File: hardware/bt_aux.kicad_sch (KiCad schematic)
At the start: 19 parts, among them J1 esp32_1, J2 AudioJack3, J2 esp32_2, U1 PCM5102A

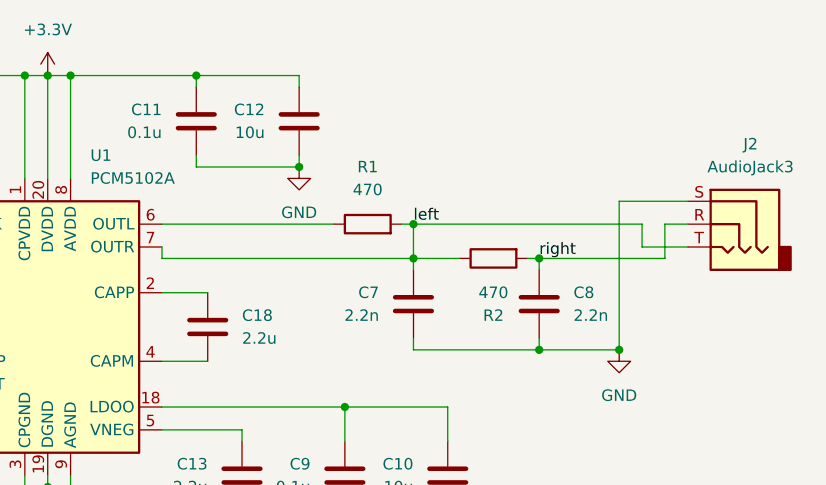
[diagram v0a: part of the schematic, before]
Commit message: update footprints, links, and price of components
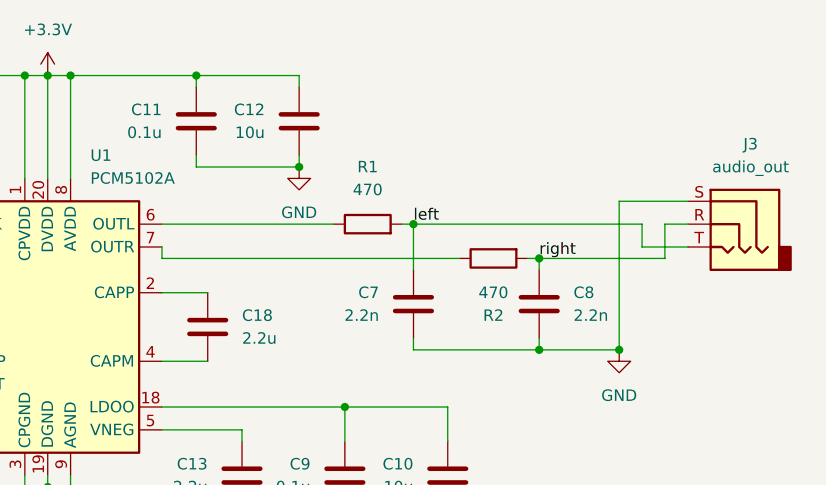
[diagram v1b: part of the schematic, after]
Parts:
- C10, C12, C15, C17: footprint (none) -> C_0805_2012Metric; Link (none) -> https://jlcpcb.com/partdetail/MurataElectronics-GRM21BR61E1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; Unit Price (none) -> $0.0168
- C11, C14, C16, C9: footprint (none) -> C_0805_2012Metric; Link (none) -> https://jlcpcb.com/partdetail/Walsin_TechCorp-0805B104K101C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; Unit Price (none) -> $0.0045
- C13, C18: footprint (none) -> C_0805_2012Metric; Link (none) -> https://jlcpcb.com/partdetail/19814-CL21B225KAFNNNE/C19110; Unit Price (none) -> $0.0128
- C7, C8: footprint (none) -> C_0805_2012Metric; Link (none) -> https://jlcpcb.com/partdetail/Walsin_TechCorp-0805N222J101C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; Unit Price (none) -> $0.0188
- J1, J2: footprint (none) -> Connector_PinSocket_2.54mm:PinSocket_1x15_P2.54mm_Vertical; Link (none) -> https://jlcpcb.com/partdetail/Hctl-PM254_1_15_Z_85/C2897378; Unit Price (none) -> $0.2109
- J3: renamed from J2; value AudioJack3 -> audio_out; footprint (none) -> audio-jack:BOOMELE_PJ-320B; Link (none) -> https://jlcpcb.com/partdetail/boomele_boom_Precision_elec-C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; Unit Price (none) -> $0.0491
- R1, R2: footprint (none) -> R_0805_2012Metric; Link (none) -> https://jlcpcb.com/partdetail/Kamaya-RMC1_10471JTP/C908864; Unit Price (none) -> $0.0019
- R3: footprint (none) -> R_0805_2012Metric; Link (none) -> https://jlcpcb.com/partdetail/18102-0805W8F1002T5E/C17414; Unit Price (none) -> $0.0013
- U1: Link (none) -> https://jlcpcb.com/partdetail/TexasInstruments-PCM5102APWR/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; Unit Price (none) -> $1.4820
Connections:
- net left: no longer R2.1, U1.7 (OUTR)
- new net: R2.1, U1.7 (OUTR)

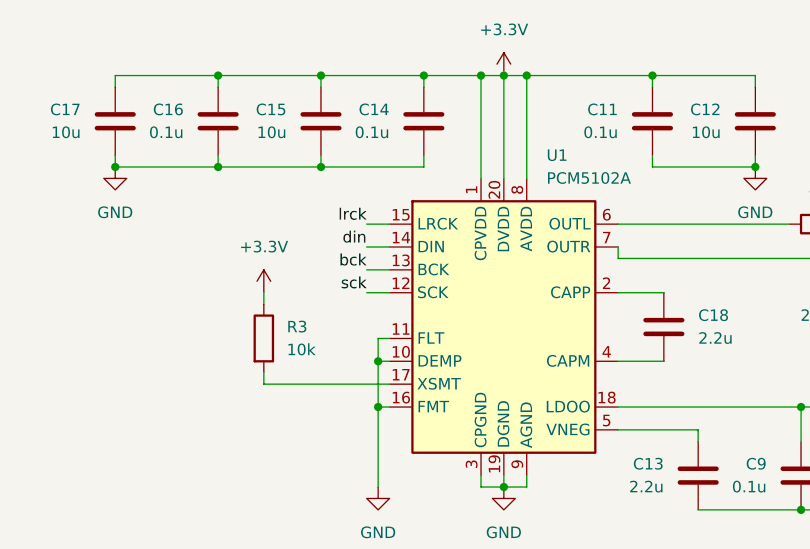
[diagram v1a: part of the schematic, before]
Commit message: change xsmt connection direct to avdd instead of pullup
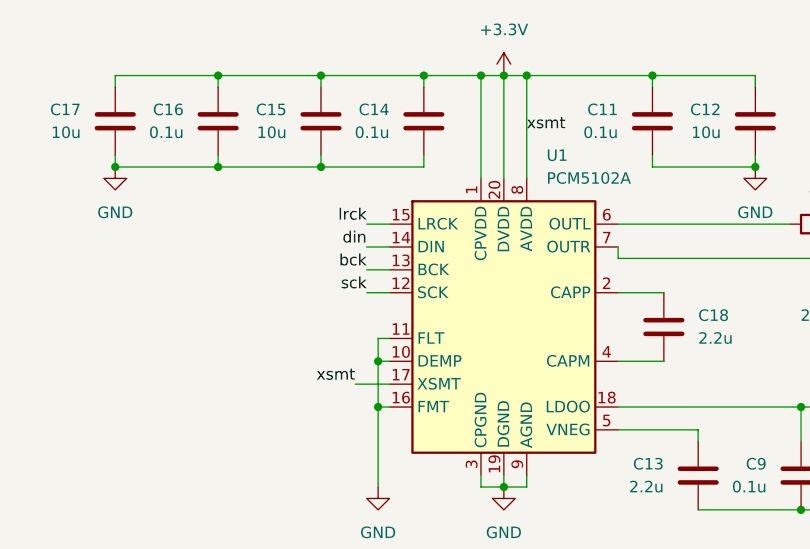
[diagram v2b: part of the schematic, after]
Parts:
- removed R3: 10k, R_0805_2012Metric, symbol Device:R
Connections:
- net +3.3V: now also U1.17 (XSMT)
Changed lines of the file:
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@@
+    (stroke (width 0) (type default))
+  )
+  (wire (pts (xy 144.78 91.44) (xy 148.59 91.44))
     (stroke (width 0) (type default))
   )
@@
     (stroke (width 0) (type default))
   )
-  (wire (pts (xy 134.62 91.44) (xy 148.59 91.44))
-    (stroke (width 0) (type default))
-  )
   (wire (pts (xy 146.05 81.28) (xy 148.59 81.28))
     (stroke (width 0) (type default))
@@
     (stroke (width 0) (type default))
   )
-  (wire (pts (xy 134.62 81.28) (xy 134.62 82.55))
-    (stroke (width 0) (type default))
-  )
   (wire (pts (xy 173.99 77.47) (xy 173.99 76.2))
     (stroke (width 0) (type default))
@@
     (stroke (width 0) (type default))
   )
-  (wire (pts (xy 134.62 90.17) (xy 134.62 91.44))
-    (stroke (width 0) (type default))
-  )
   (wire (pts (xy 227.33 73.66) (xy 201.93 73.66))
     (stroke (width 0) (type default))
@@
   (label "lrck" (at 46.99 88.9 180) (fields_autoplaced)
     (effects (font (size 1.27 1.27)) (justify right bottom))
+  )
+  (label "xsmt" (at 163.83 63.5 0) (fields_autoplaced)
+    (effects (font (size 1.27 1.27)) (justify left bottom))
   )
   (label "bck" (at 46.99 93.98 180) (fields_autoplaced)
@@
   )
   (label "din" (at 46.99 91.44 180) (fields_autoplaced)
+    (effects (font (size 1.27 1.27)) (justify right bottom))
+  )
+  (label "xsmt" (at 144.78 91.44 180) (fields_autoplaced)
     (effects (font (size 1.27 1.27)) (justify right bottom))
   )
@@
     )
   )
-  (symbol (lib_id "power:+3.3V") (at 134.62 81.28 0) (unit 1)
-    (in_bom yes) (on_board yes) (dnp no) (fields_autoplaced)
-    (property "Reference" "#PWR06" (at 134.62 85.09 0)
-      (effects (font (size 1.27 1.27)) hide)
-    )
-    (property "Value" "+3.3V" (at 134.62 76.2 0)
-      (effects (font (size 1.27 1.27)))
-    )
-    (property "Footprint" "" (at 134.62 81.28 0)
-      (effects (font (size 1.27 1.27)) hide)
-    )
-    (property "Datasheet" "" (at 134.62 81.28 0)
-      (effects (font (size 1.27 1.27)) hide)
-    )
-    (pin "1")
-    (instances
-      (project "bt_aux"
-        (path "/cca713bf-7872-426b-918e-02310faf0ed4"
-          (reference "#PWR06") (unit 1)
-        )
-      )
-    )
-  )
   (symbol (lib_id "Device:C") (at 129.54 62.23 0) (unit 1)
     (in_bom yes) (on_board yes) (dnp no)
@@
         )
       )
-    )
-  )
-  (symbol (lib_id "Device:R") (at 134.62 86.36 0) (unit 1)
-    (in_bom yes) (on_board yes) (dnp no) (fields_autoplaced)
-    (property "Reference" "R3" (at 137.16 85.09 0)
-      (effects (font (size 1.27 1.27)) (justify left))
-    )
-    (property "Value" "10k" (at 137.16 87.63 0)
-      (effects (font (size 1.27 1.27)) (justify left))
-    )
-    (property "Footprint" "R_0805_2012Metric" (at 132.842 86.36 90)
-      (effects (font (size 1.27 1.27)) hide)
-    )
-    (property "Datasheet" "~" (at 134.62 86.36 0)
-      (effects (font (size 1.27 1.27)) hide)
-    )
-    (property "Link" "https://jlcpcb.com/partdetail/18102-0805W8F1002T5E/C17414" (at 134.62 86.36 0)
-      (effects (font (size 1.27 1.27)) hide)
-    )
-    (property "Unit Price" " $0.0013 " (at 134.62 86.36 0)
-      (effects (font (size 1.27 1.27)) hide)
-    )
-    (pin "2")
-    (pin "1")
-    (instances
-      (project "bt_aux"
-        (path "/cca713bf-7872-426b-918e-02310faf0ed4"
-          (reference "R3") (unit 1)
-        )
-      )

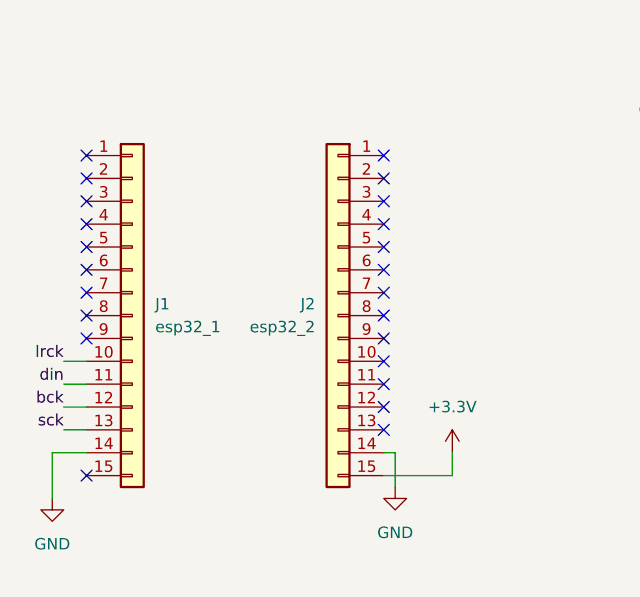
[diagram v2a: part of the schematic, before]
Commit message: add copper pours and rest of connections to headers
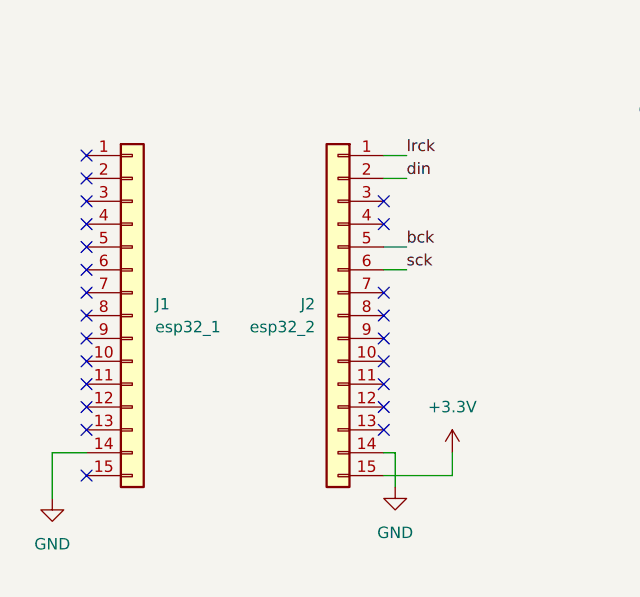
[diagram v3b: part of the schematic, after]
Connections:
- net bck: now also J2.5 (Pin_5); no longer J1.12 (Pin_12)
- net din: now also J2.2 (Pin_2); no longer J1.11 (Pin_11)
- net lrck: now also J2.1 (Pin_1); no longer J1.10 (Pin_10)
- net sck: now also J2.6 (Pin_6); no longer J1.13 (Pin_13)
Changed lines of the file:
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@@
   )
   (no_connect (at 82.55 96.52))
-  (no_connect (at 82.55 66.04))
   (no_connect (at 82.55 91.44))
   (no_connect (at 82.55 86.36))
@@
   (no_connect (at 82.55 93.98))
   (no_connect (at 49.53 78.74))
+  (no_connect (at 49.53 93.98))
   (no_connect (at 49.53 81.28))
   (no_connect (at 82.55 83.82))
   (no_connect (at 49.53 86.36))
-  (no_connect (at 82.55 78.74))
-  (no_connect (at 82.55 68.58))
+  (no_connect (at 49.53 88.9))
   (no_connect (at 82.55 71.12))
   (no_connect (at 49.53 76.2))
@@
   (no_connect (at 82.55 73.66))
   (no_connect (at 82.55 88.9))
+  (no_connect (at 49.53 96.52))
   (no_connect (at 49.53 66.04))
+  (no_connect (at 49.53 91.44))
   (no_connect (at 49.53 71.12))
-  (no_connect (at 82.55 76.2))
   (wire (pts (xy 205.74 97.79) (xy 205.74 93.98))
     (stroke (width 0) (type default))
@@
     (stroke (width 0) (type default))
   )
-  (wire (pts (xy 46.99 96.52) (xy 49.53 96.52))
-    (stroke (width 0) (type default))
-  )
   (wire (pts (xy 146.05 78.74) (xy 148.59 78.74))
     (stroke (width 0) (type default))
@@
     (stroke (width 0) (type default))
   )
+  (wire (pts (xy 85.09 68.58) (xy 82.55 68.58))
+    (stroke (width 0) (type default))
+  )
   (wire (pts (xy 182.88 97.79) (xy 182.88 96.52))
     (stroke (width 0) (type default))
@@
     (stroke (width 0) (type default))
   )
+  (wire (pts (xy 85.09 78.74) (xy 82.55 78.74))
+    (stroke (width 0) (type default))
+  )
   (wire (pts (xy 173.99 96.52) (xy 182.88 96.52))
     (stroke (width 0) (type default))
@@
     (stroke (width 0) (type default))
   )
+  (wire (pts (xy 85.09 76.2) (xy 82.55 76.2))
+    (stroke (width 0) (type default))
+  )
   (wire (pts (xy 152.4 57.15) (xy 152.4 58.42))
     (stroke (width 0) (type default))
@@
     (stroke (width 0) (type default))
   )
-  (wire (pts (xy 46.99 93.98) (xy 49.53 93.98))
-    (stroke (width 0) (type default))
-  )
   (wire (pts (xy 158.75 102.87) (xy 158.75 101.6))
     (stroke (width 0) (type default))
@@
     (stroke (width 0) (type default))
   )
+  (wire (pts (xy 85.09 66.04) (xy 82.55 66.04))
+    (stroke (width 0) (type default))
+  )
   (wire (pts (xy 148.59 86.36) (xy 147.32 86.36))
     (stroke (width 0) (type default))
@@
     (stroke (width 0) (type default))
   )
-  (wire (pts (xy 46.99 91.44) (xy 49.53 91.44))
-    (stroke (width 0) (type default))
-  )
   (wire (pts (xy 182.88 105.41) (xy 194.31 105.41))
     (stroke (width 0) (type default))
@@
     (stroke (width 0) (type default))
   )
-  (wire (pts (xy 46.99 88.9) (xy 49.53 88.9))
-    (stroke (width 0) (type default))
+  (label "din" (at 85.09 68.58 0) (fields_autoplaced)
+    (effects (font (size 1.27 1.27)) (justify left bottom))
   )
   (label "sck" (at 146.05 81.28 180) (fields_autoplaced)
     (effects (font (size 1.27 1.27)) (justify right bottom))
   )
-  (label "lrck" (at 46.99 88.9 180) (fields_autoplaced)
-    (effects (font (size 1.27 1.27)) (justify right bottom))
+  (label "lrck" (at 85.09 66.04 0) (fields_autoplaced)
+    (effects (font (size 1.27 1.27)) (justify left bottom))
   )
   (label "xsmt" (at 163.83 63.5 0) (fields_autoplaced)
     (effects (font (size 1.27 1.27)) (justify left bottom))
   )
-  (label "bck" (at 46.99 93.98 180) (fields_autoplaced)
-    (effects (font (size 1.27 1.27)) (justify right bottom))
-  )
   (label "right" (at 215.9 77.47 0) (fields_autoplaced)
     (effects (font (size 1.27 1.27)) (justify left bottom))
   )
+  (label "bck" (at 85.09 76.2 0) (fields_autoplaced)
+    (effects (font (size 1.27 1.27)) (justify left bottom))
+  )
+  (label "sck" (at 85.09 78.74 0) (fields_autoplaced)
+    (effects (font (size 1.27 1.27)) (justify left bottom))
+  )
   (label "din" (at 146.05 76.2 180) (fields_autoplaced)
     (effects (font (size 1.27 1.27)) (justify right bottom))
   )
-  (label "din" (at 46.99 91.44 180) (fields_autoplaced)
-    (effects (font (size 1.27 1.27)) (justify right bottom))
-  )
   (label "xsmt" (at 144.78 91.44 180) (fields_autoplaced)
     (effects (font (size 1.27 1.27)) (justify right bottom))
@@
     (effects (font (size 1.27 1.27)) (justify right bottom))
   )
-  (label "sck" (at 46.99 96.52 180) (fields_autoplaced)
-    (effects (font (size 1.27 1.27)) (justify right bottom))
-  )

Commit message: modify bom, generate fab files, submit order
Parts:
- C10, C12, C15, C17: LCSC (none) -> C84416; Link https://jlcpcb.com/partdetail/MurataElectronics-GRM21BR61E1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 -> (none); Unit Price $0.0168 -> (none)
- C11, C14, C16, C9: LCSC (none) -> C77456; Link https://jlcpcb.com/partdetail/Walsin_TechCorp-0805B104K101C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 -> (none); Unit Price $0.0045 -> (none)
- C13, C18: LCSC (none) -> C19110; Link https://jlcpcb.com/partdetail/19814-CL21B225KAFNNNE/C19110 -> (none); Unit Price $0.0128 -> (none)
- C7, C8: LCSC (none) -> C2875527; Link https://jlcpcb.com/partdetail/Walsin_TechCorp-0805N222J101C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 -> (none); Unit Price $0.0188 -> (none)
- J1, J2: LCSC (none) -> C2897378; Link https://jlcpcb.com/partdetail/Hctl-PM254_1_15_Z_85/C2897378 -> (none); Unit Price $0.2109 -> (none)
- J3: LCSC (none) -> C18594; Link https://jlcpcb.com/partdetail/boomele_boom_Precision_elec-C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 -> (none); Unit Price $0.0491 -> (none)
- R1, R2: LCSC (none) -> C908864; Link https://jlcpcb.com/partdetail/Kamaya-RMC1_10471JTP/C908864 -> (none); Unit Price $0.0019 -> (none)
- U1: LCSC (none) -> C107671; Link https://jlcpcb.com/partdetail/TexasInstruments-PCM5102APWR/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 -> (none); Unit Price $1.4820 -> (none)
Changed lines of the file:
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@@
       (effects (font (size 1.27 1.27)) hide)
     )
-    (property "Link" "https://jlcpcb.com/partdetail/TexasInstruments-PCM5102APWR/C107671" (at 161.29 83.82 0)
-      (effects (font (size 1.27 1.27)) hide)
-    )
-    (property "Unit Price" " $1.4820 " (at 161.29 83.82 0)
+    (property "LCSC" "C107671" (at 161.29 83.82 0)
       (effects (font (size 1.27 1.27)) hide)
     )
@@
       (effects (font (size 1.27 1.27)) hide)
     )
-    (property "Link" "https://jlcpcb.com/partdetail/Hctl-PM254_1_15_Z_85/C2897378" (at 54.61 83.82 0)
-      (effects (font (size 1.27 1.27)) hide)
-    )
-    (property "Unit Price" " $0.2109 " (at 54.61 83.82 0)
+    (property "LCSC" "C2897378" (at 54.61 83.82 0)
       (effects (font (size 1.27 1.27)) hide)
     )
@@
       (effects (font (size 1.27 1.27)) hide)
     )
-    (property "Link" "https://jlcpcb.com/partdetail/Kamaya-RMC1_10471JTP/C908864" (at 210.82 77.47 0)
-      (effects (font (size 1.27 1.27)) hide)
-    )
-    (property "Unit Price" "$0.0019" (at 210.82 77.47 0)
+    (property "LCSC" "C908864" (at 210.82 77.47 0)
       (effects (font (size 1.27 1.27)) hide)
     )
@@
       (effects (font (size 1.27 1.27)) hide)
     )
-    (property "Link" "https://jlcpcb.com/partdetail/Walsin_TechCorp-0805B104K101CT/C77456" (at 129.54 62.23 0)
-      (effects (font (size 1.27 1.27)) hide)
-    )
-    (property "Unit Price" " $0.0045 " (at 129.54 62.23 0)
+    (property "LCSC" "C77456" (at 129.54 62.23 0)
       (effects (font (size 1.27 1.27)) hide)
     )
@@
       (effects (font (size 1.27 1.27)) hide)
     )
-    (property "Link" "https://jlcpcb.com/partdetail/Walsin_TechCorp-0805B104K101CT/C77456" (at 152.4 62.23 0)
-      (effects (font (size 1.27 1.27)) hide)
-    )
-    (property "Unit Price" " $0.0045 " (at 152.4 62.23 0)
+    (property "LCSC" "C77456" (at 152.4 62.23 0)
       (effects (font (size 1.27 1.27)) hide)
     )
@@
       (effects (font (size 1.27 1.27)) hide)
     )
-    (property "Link" "https://jlcpcb.com/partdetail/Walsin_TechCorp-0805B104K101CT/C77456" (at 194.31 101.6 0)
-      (effects (font (size 1.27 1.27)) hide)
-    )
-    (property "Unit Price" " $0.0045 " (at 194.31 101.6 0)
+    (property "LCSC" "C77456" (at 194.31 101.6 0)
       (effects (font (size 1.27 1.27)) hide)
     )
@@
       (effects (font (size 1.27 1.27)) hide)
     )
-    (property "Link" "https://jlcpcb.com/partdetail/19814-CL21B225KAFNNNE/C19110" (at 182.88 101.6 0)
-      (effects (font (size 1.27 1.27)) hide)
-    )
-    (property "Unit Price" " $0.0128 " (at 182.88 101.6 0)
+    (property "LCSC" "C19110" (at 182.88 101.6 0)
       (effects (font (size 1.27 1.27)) hide)
     )
@@
       (effects (font (size 1.27 1.27)) hide)
     )
-    (property "Link" "https://jlcpcb.com/partdetail/Walsin_TechCorp-0805B104K101CT/C77456" (at 177.8 62.23 0)
-      (effects (font (size 1.27 1.27)) hide)
-    )
-    (property "Unit Price" " $0.0045 " (at 177.8 62.23 0)
+    (property "LCSC" "C77456" (at 177.8 62.23 0)
       (effects (font (size 1.27 1.27)) hide)
     )
@@
       (effects (font (size 1.27 1.27)) hide)
     )
-    (property "Link" "https://jlcpcb.com/partdetail/MurataElectronics-GRM21BR61E106KA73L/C84416" (at 118.11 62.23 0)
-      (effects (font (size 1.27 1.27)) hide)
-    )
-    (property "Unit Price" " $0.0168 " (at 118.11 62.23 0)
+    (property "LCSC" "C84416" (at 118.11 62.23 0)
       (effects (font (size 1.27 1.27)) hide)
     )
@@
       (effects (font (size 1.27 1.27)) hide)
     )
-    (property "Link" "https://jlcpcb.com/partdetail/MurataElectronics-GRM21BR61E106KA73L/C84416" (at 205.74 101.6 0)
-      (effects (font (size 1.27 1.27)) hide)
-    )
-    (property "Unit Price" " $0.0168 " (at 205.74 101.6 0)
+    (property "LCSC" "C84416" (at 205.74 101.6 0)
       (effects (font (size 1.27 1.27)) hide)
     )
@@
       (effects (font (size 1.27 1.27)) hide)
     )
-    (property "Link" "https://jlcpcb.com/partdetail/Walsin_TechCorp-0805N222J101CT/C2875527" (at 201.93 82.55 0)
-      (effects (font (size 1.27 1.27)) hide)
-    )
-    (property "Unit Price" " $0.0188 " (at 201.93 82.55 0)
+    (property "LCSC" "C2875527" (at 201.93 82.55 0)
       (effects (font (size 1.27 1.27)) hide)
     )
@@
       (effects (font (size 1.27 1.27)) hide)
     )
-    (property "Link" "https://jlcpcb.com/partdetail/Walsin_TechCorp-0805N222J101CT/C2875527" (at 215.9 82.55 0)
-      (effects (font (size 1.27 1.27)) hide)
-    )
-    (property "Unit Price" " $0.0188 " (at 215.9 82.55 0)
+    (property "LCSC" "C2875527" (at 215.9 82.55 0)
       (effects (font (size 1.27 1.27)) hide)
     )
@@
       (effects (font (size 1.27 1.27)) hide)
     )
-    (property "Link" "https://jlcpcb.com/partdetail/boomele_boom_Precision_elec-C18594/C18594" (at 237.49 73.66 0)
-      (effects (font (size 1.27 1.27)) hide)
-    )
-    (property "Unit Price" " $0.0491 " (at 237.49 73.66 0)
+    (property "LCSC" "C18594" (at 237.49 73.66 0)
       (effects (font (size 1.27 1.27)) hide)
     )
@@
       (effects (font (size 1.27 1.27)) hide)
     )
-    (property "Link" "https://jlcpcb.com/partdetail/MurataElectronics-GRM21BR61E106KA73L/C84416" (at 189.23 62.23 0)
-      (effects (font (size 1.27 1.27)) hide)
-    )
-    (property "Unit Price" " $0.0168 " (at 189.23 62.23 0)
+    (property "LCSC" "C84416" (at 189.23 62.23 0)
       (effects (font (size 1.27 1.27)) hide)
     )
@@
       (effects (font (size 1.27 1.27)) hide)
     )
-    (property "Link" "https://jlcpcb.com/partdetail/19814-CL21B225KAFNNNE/C19110" (at 179.07 85.09 0)
-      (effects (font (size 1.27 1.27)) hide)
-    )
-    (property "Unit Price" " $0.0128 " (at 179.07 85.09 0)
+    (property "LCSC" "C19110" (at 179.07 85.09 0)
       (effects (font (size 1.27 1.27)) hide)
     )
@@
       (effects (font (size 1.27 1.27)) hide)
     )
-    (property "Link" "https://jlcpcb.com/partdetail/Hctl-PM254_1_15_Z_85/C2897378" (at 77.47 83.82 0)
-      (effects (font (size 1.27 1.27)) hide)
-    )
-    (property "Unit Price" " $0.2109 " (at 77.47 83.82 0)
+    (property "LCSC" "C2897378" (at 77.47 83.82 0)
       (effects (font (size 1.27 1.27)) hide)
     )
@@
       (effects (font (size 1.27 1.27)) hide)
     )
-    (property "Link" "https://jlcpcb.com/partdetail/MurataElectronics-GRM21BR61E106KA73L/C84416" (at 140.97 62.23 0)
-      (effects (font (size 1.27 1.27)) hide)
-    )
-    (property "Unit Price" " $0.0168 " (at 140.97 62.23 0)
+    (property "LCSC" "C84416" (at 140.97 62.23 0)
       (effects (font (size 1.27 1.27)) hide)
     )
@@
       (effects (font (size 1.27 1.27)) hide)
     )
-    (property "Link" "https://jlcpcb.com/partdetail/Kamaya-RMC1_10471JTP/C908864" (at 196.85 73.66 0)
-      (effects (font (size 1.27 1.27)) hide)
-    )
-    (property "Unit Price" "$0.0019" (at 196.85 73.66 0)
-      (effects (font (size 1.27 1.27)) hide)
-    )
+    (property "LCSC" "C908864" (at 196.85 73.66 0)
+      (effects (font (size 1.27 1.27)) hide)
+    )
